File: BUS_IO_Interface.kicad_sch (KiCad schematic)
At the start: 21 parts, among them U12 MAX31331TETB+, U13 AS1016204-0108X0PWAY, U14 TCAN1044ADDFRQ1, Y3 32.768kHz

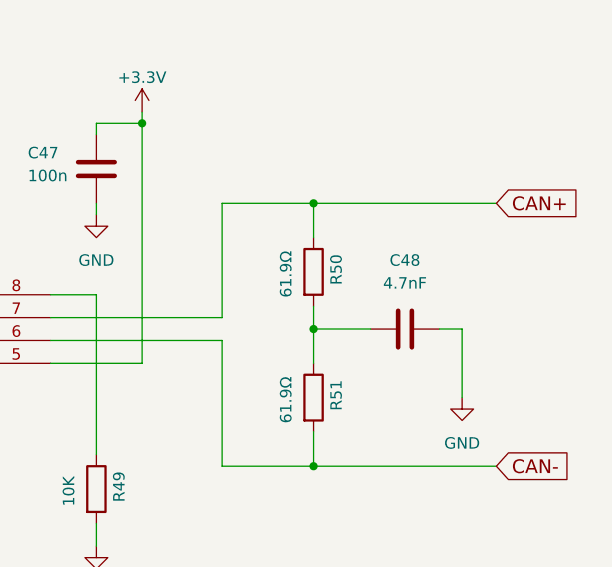
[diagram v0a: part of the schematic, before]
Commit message: Fix values of a lot of parts
Make them standard, 4.1p instead of 4p1, etc.

Add a tag to a couple of ICs that didn't have a pin 1 indicator on the
board.

Signed-off-by: Corey Minyard <corey@minyard.net>
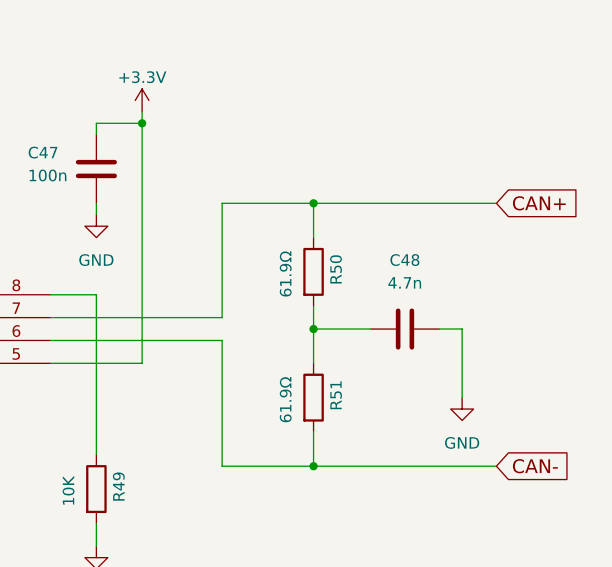
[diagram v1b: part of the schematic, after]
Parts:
- C48: value 4.7nF -> 4.7n
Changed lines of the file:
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@@
 			)
 		)
-		(property "Value" "4.7nF"
+		(property "Value" "4.7n"
 			(at 358.14 91.44 90)
 			(effects

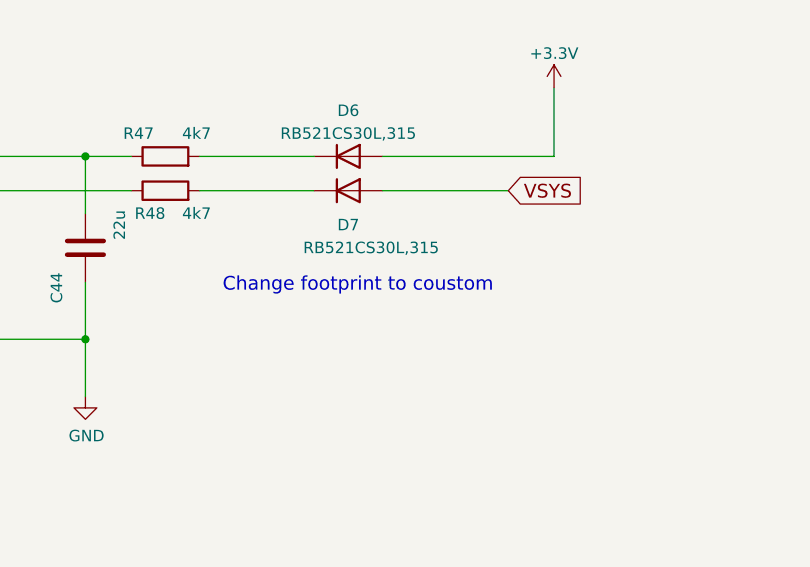
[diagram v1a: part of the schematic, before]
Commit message: Add some notes, fix the diode footprints on the RTC
Signed-off-by: Corey Minyard <corey@minyard.net>
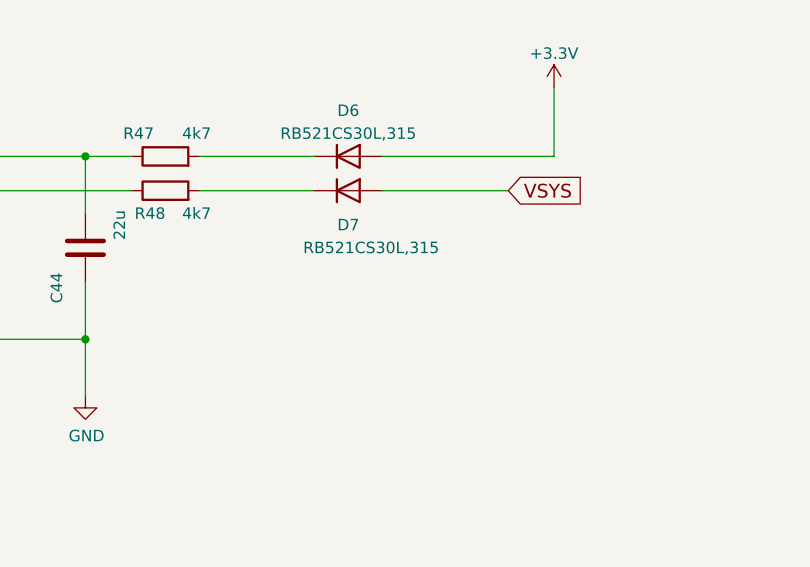
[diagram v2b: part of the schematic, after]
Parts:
- D6, D7: footprint Diode_SMD:D_0603_1608Metric -> Diode_SMD:D_SOD-882
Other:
- note removed: "Change footprint to coustom"
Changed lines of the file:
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@@
 		)
 	)
-	(text "Change footprint to coustom"
-		(exclude_from_sim no)
-		(at 186.69 161.29 0)
-		(effects
-			(font
-				(size 1.524 1.524)
-			)
-			(justify left bottom)
-		)
-	)
 	(text "Real Time Clock"
 		(exclude_from_sim no)
@@
 			)
 		)
-		(property "Footprint" "Diode_SMD:D_0603_1608Metric"
+		(property "Footprint" "Diode_SMD:D_SOD-882"
 			(at 200.66 150.495 0)
 			(effects
@@
 			)
 		)
-		(property "Footprint" "Diode_SMD:D_0603_1608Metric"
+		(property "Footprint" "Diode_SMD:D_SOD-882"
 			(at 200.66 154.305 0)
 			(effects

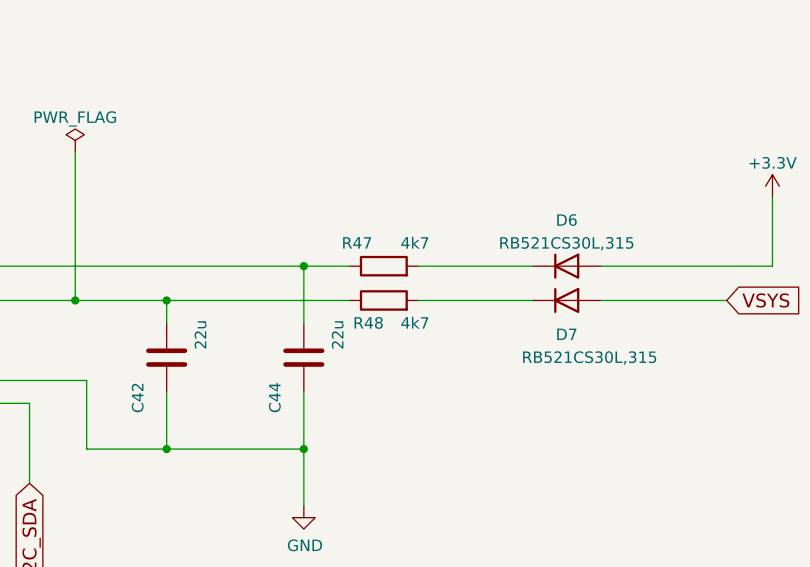
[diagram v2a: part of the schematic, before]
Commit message: Update ferrite beads with actual values
Signed-off-by: Corey Minyard <corey@minyard.net>
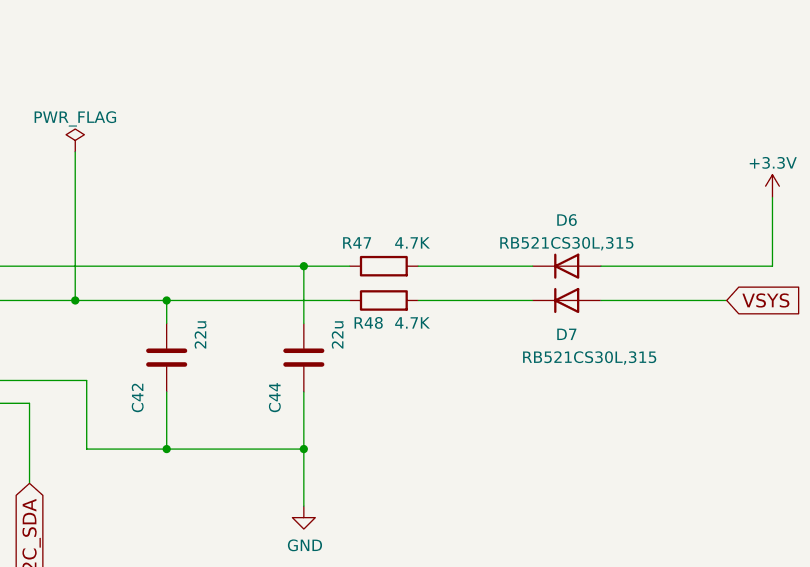
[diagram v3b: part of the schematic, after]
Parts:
- R47, R48: value 4k7 -> 4.7K
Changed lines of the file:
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@@
 			)
 		)
-		(property "Value" "4k7"
+		(property "Value" "4.7K"
 			(at 185.42 143.51 90)
 			(effects
@@
 			)
 		)
-		(property "Value" "4k7"
+		(property "Value" "4.7K"
 			(at 185.42 152.4 90)
 			(effects

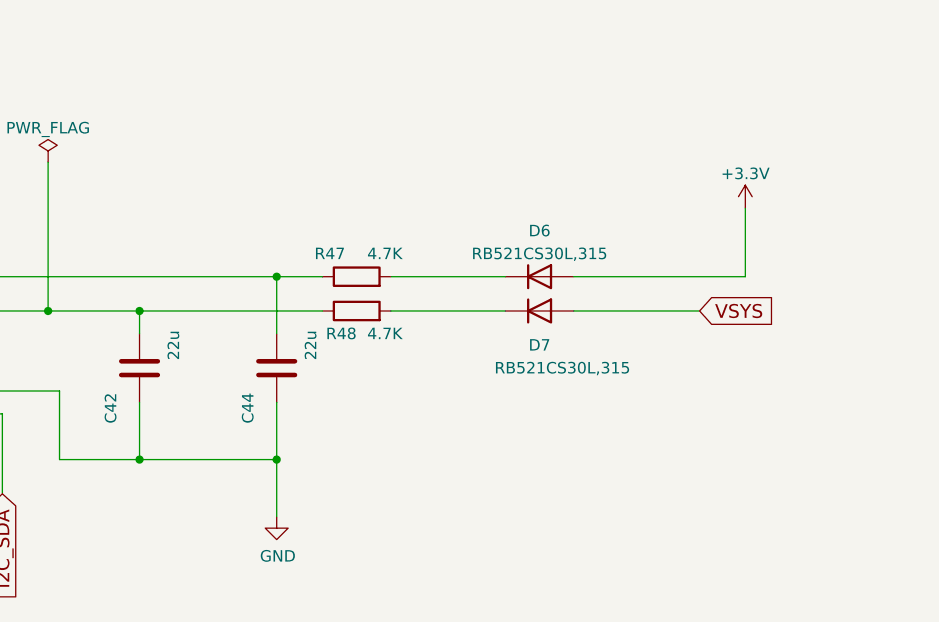
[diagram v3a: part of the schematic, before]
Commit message: Move the RTC and rework it a bit
Signed-off-by: Corey Minyard <corey@minyard.net>
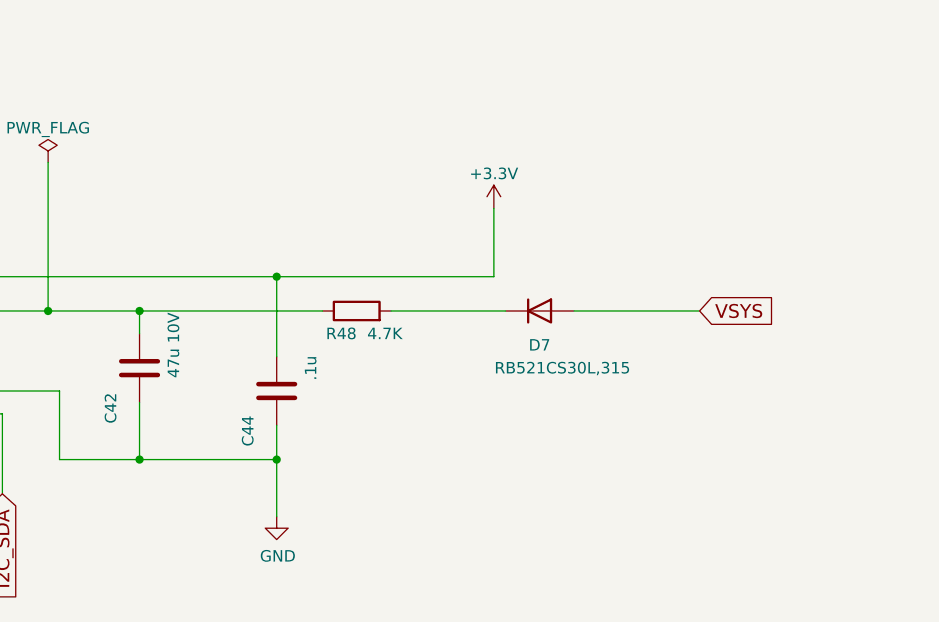
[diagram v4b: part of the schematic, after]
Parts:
- removed D6: RB521CS30L,315, Diode_SMD:D_SOD-882, symbol Diode:1N914
- removed R47: 4.7K, Resistor_SMD:R_0603_1608Metric_Pad0.98x0.95mm_HandSolder, symbol Device:R
- C42: value 22u -> 47u 10V; footprint Capacitor_SMD:C_0603_1608Metric_Pad1.08x0.95mm_HandSolder -> Capacitor_SMD:C_0805_2012Metric_Pad1.18x1.45mm_HandSolder
- C44: value 22u -> .1u
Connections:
- net +3.3V: now also C44.1, U12.10 (VCC)
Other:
- moved on the sheet: C44
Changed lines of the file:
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@@
-	(wire
-		(pts
-			(xy 184.15 146.05) (xy 196.85 146.05)
-		)
-		(stroke
-			(width 0)
-			(type default)
-		)
-	)
 	(wire
 		(pts
@@
 	(wire
 		(pts
-			(xy 171.45 146.05) (xy 176.53 146.05)
+			(xy 171.45 146.05) (xy 195.58 146.05)
 		)
 		(stroke
@@
 	(wire
 		(pts
-			(xy 171.45 146.05) (xy 171.45 152.4)
+			(xy 171.45 146.05) (xy 171.45 154.94)
 		)
 		(stroke
@@
 	(wire
 		(pts
-			(xy 171.45 166.37) (xy 171.45 160.02)
+			(xy 171.45 166.37) (xy 171.45 162.56)
 		)
 		(stroke
@@
 	(wire
 		(pts
-			(xy 223.52 146.05) (xy 223.52 138.43)
+			(xy 195.58 146.05) (xy 195.58 138.43)
 		)
 		(stroke
@@
 		(pts
 			(xy 92.71 147.32) (xy 92.71 134.62)
-		)
-		(stroke
-			(width 0)
-			(type default)
-		)
-	)
-	(wire
-		(pts
-			(xy 204.47 146.05) (xy 223.52 146.05)
 		)
 		(stroke
@@
 			)
 		)
-		(property "Value" "22u"
+		(property "Value" "47u 10V"
 			(at 160.02 153.67 90)
 			(effects
@@
 			)
 		)
-		(property "Footprint" "Capacitor_SMD:C_0603_1608Metric_Pad1.08x0.95mm_HandSolder"
+		(property "Footprint" "Capacitor_SMD:C_0805_2012Metric_Pad1.18x1.45mm_HandSolder"
 			(at 157.1752 160.02 0)
 			(effects
@@
 	)
 	(symbol
-		(lib_id "Device:R")
-		(at 180.34 146.05 90)
-		(unit 1)
-		(exclude_from_sim no)
-		(in_bom yes)
-		(on_board yes)
-		(dnp no)
-		(property "Reference" "R47"
-			(at 179.07 143.51 90)
-			(effects
-				(font
-					(size 1.27 1.27)
-				)
-				(justify left)
-			)
-		)
-		(property "Value" "4.7K"
-			(at 185.42 143.51 90)
-			(effects
-				(font
-					(size 1.27 1.27)
-				)
-				(justify left)
-			)
-		)
-		(property "Footprint" "Resistor_SMD:R_0603_1608Metric_Pad0.98x0.95mm_HandSolder"
-			(at 180.34 147.828 90)
-			(effects
-				(font
-					(size 1.27 1.27)
-				)
-				(hide yes)
-			)
-		)
-		(property "Datasheet" "~"
-			(at 180.34 146.05 0)
-			(effects
-				(font
-					(size 1.27 1.27)
-				)
-			)
-		)
-		(property "Description" ""
-			(at 180.34 146.05 0)
-			(effects
-				(font
-					(size 1.27 1.27)
-				)
-			)
-		)
-		(pin "1"
-		)
-		(pin "2"
-		)
-		(instances
-			(project "PacSat_Dev_RevD_240614"
-				(path "/cc9f42d2-6985-41ac-acab-5ab7b01c5b38/aff81ec5-748c-4fc9-b1e8-df12a16f6289"
-					(reference "R47")
-					(unit 1)
-				)
-			)
-		)
-	)
-	(symbol
 		(lib_id "PACSAT_ICs:MAX31331")
 		(at 110.49 154.94 0)
@@
 	(symbol
 		(lib_id "Device:C")
-		(at 171.45 156.21 0)
+		(at 171.45 158.75 0)
 		(unit 1)
 		(exclude_from_sim no)
@@
 		(dnp no)
 		(property "Reference" "C44"
-			(at 168.275 160.655 90)
-			(effects
-				(font
-					(size 1.27 1.27)
-				)
-			)
-		)
-		(property "Value" "22u"
-			(at 175.26 153.67 90)
+			(at 168.275 163.195 90)
+			(effects
+				(font
+					(size 1.27 1.27)
+				)
+			)
+		)
+		(property "Value" ".1u"
+			(at 175.26 156.21 90)
 			(effects
 				(font
@@
 		)
 		(property "Footprint" "Capacitor_SMD:C_0603_1608Metric_Pad1.08x0.95mm_HandSolder"
-			(at 172.4152 160.02 0)
+			(at 172.4152 162.56 0)
 			(effects
 				(font
@@
 		)
 		(property "Datasheet" "~"
-			(at 171.45 156.21 0)
+			(at 171.45 158.75 0)
 			(effects
 				(font
@@
 		)
 		(property "Description" ""
-			(at 171.45 156.21 0)
+			(at 171.45 158.75 0)
 			(effects
 				(font
@@
 	)
 	(symbol
-		(lib_id "Diode:1N914")
-		(at 200.66 146.05 0)
-		(unit 1)
-		(exclude_from_sim no)
-		(in_bom yes)
-		(on_board yes)
-		(dnp no)
-		(fields_autoplaced yes)
-		(property "Reference" "D6"
-			(at 200.66 140.97 0)
-			(effects
-				(font
-					(size 1.27 1.27)
-				)
-			)
-		)
-		(property "Value" "RB521CS30L,315"
-			(at 200.66 143.51 0)
-			(effects
-				(font
-					(size 1.27 1.27)
-				)
-			)
-		)
-		(property "Footprint" "Diode_SMD:D_SOD-882"
-			(at 200.66 150.495 0)
-			(effects
-				(font
-					(size 1.27 1.27)
-				)
-				(hide yes)
-			)
-		)
-		(property "Datasheet" "http://www.vishay.com/docs/85622/1n914.pdf"
-			(at 200.66 146.05 0)
-			(effects
-				(font
-					(size 1.27 1.27)
-				)
-				(hide yes)
-			)
-		)
-		(property "Description" ""
-			(at 200.66 146.05 0)
-			(effects
-				(font
-					(size 1.27 1.27)
-				)
-			)
-		)
-		(property "Sim.Device" "D"
-			(at 200.66 146.05 0)
-			(effects
-				(font
-					(size 1.27 1.27)
-				)
-				(hide yes)
-			)
-		)
-		(property "Sim.Pins" "1=K 2=A"
-			(at 200.66 146.05 0)
-			(effects
-				(font
-					(size 1.27 1.27)
-				)
-				(hide yes)
-			)
-		)
-		(pin "1"
-		)
-		(pin "2"
-		)
-		(instances
-			(project "PacSat_Dev_RevD_240614"
-				(path "/cc9f42d2-6985-41ac-acab-5ab7b01c5b38/aff81ec5-748c-4fc9-b1e8-df12a16f6289"
-					(reference "D6")
-					(unit 1)
-				)
-			)
-		)
-	)
-	(symbol
 		(lib_id "PACSAT_ICs:QSPI_FLASH_WSON_8-pin")
 		(at 133.35 64.77 0)
@@
 	(symbol
 		(lib_id "power:+3.3V")
-		(at 223.52 138.43 0)
+		(at 195.58 138.43 0)
 		(unit 1)
 		(exclude_from_sim no)
@@
 		(fields_autoplaced yes)
 		(property "Reference" "#PWR0113"
-			(at 223.52 142.24 0)
+			(at 195.58 142.24 0)
 			(effects
 				(font
@@
 		)
 		(property "Value" "+3.3V"
-			(at 223.52 134.62 0)
+			(at 195.58 134.62 0)
 			(effects
 				(font
@@
 		)
 		(property "Footprint" ""
-			(at 223.52 138.43 0)
+			(at 195.58 138.43 0)
 			(effects
 				(font
@@
 		)
 		(property "Datasheet" ""
-			(at 223.52 138.43 0)
+			(at 195.58 138.43 0)
 			(effects
 				(font
@@
 		)
 		(property "Description" ""
-			(at 223.52 138.43 0)
-			(effects
-				(font
+			(at 195.58 138.43 0)
+			(effects
+				(font

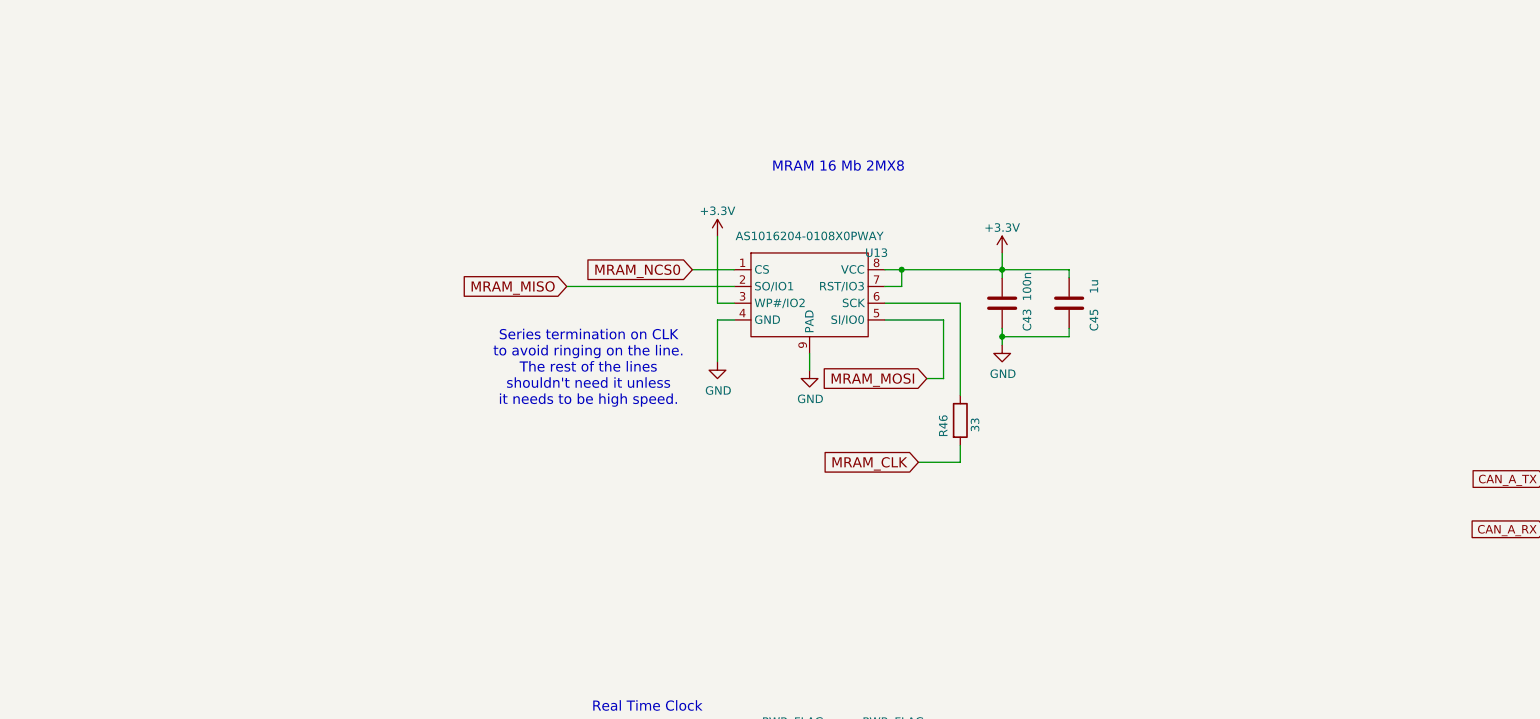
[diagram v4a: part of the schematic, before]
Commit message: Add 4 more MRAM parts
Signed-off-by: Corey Minyard <corey@minyard.net>
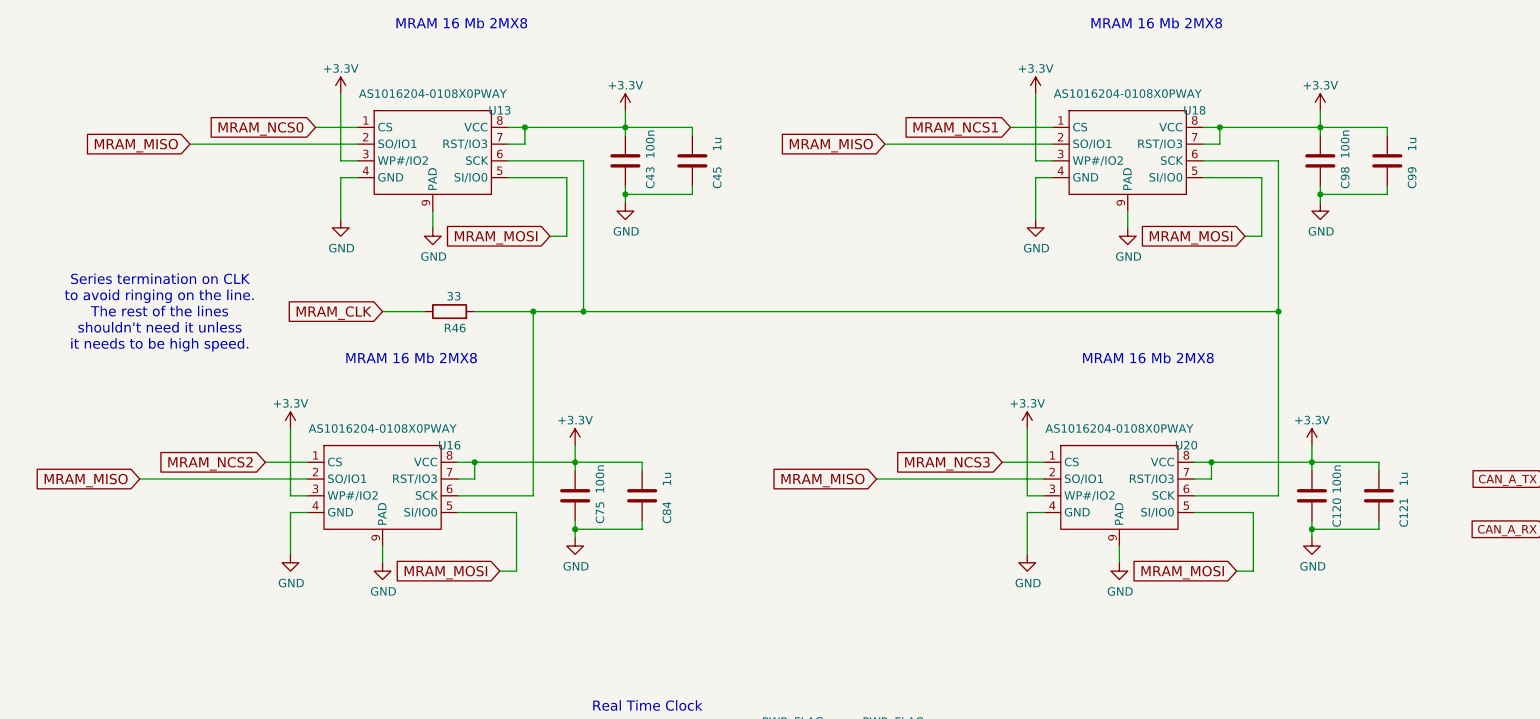
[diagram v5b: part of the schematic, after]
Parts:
- added C120, C75, C98: 100n, Capacitor_SMD:C_0603_1608Metric_Pad1.08x0.95mm_HandSolder, symbol Device:C
- added C121, C84, C99: 1u, Capacitor_SMD:C_0603_1608Metric_Pad1.08x0.95mm_HandSolder, symbol Device:C
- added U16, U18, U20: AS1016204-0108X0PWAY, Package_SON:WSON-8-1EP_8x6mm_P1.27mm_EP3.4x4.3mm, symbol PACSAT_ICs:QSPI_FLASH_WSON_8-pin
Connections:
- net +3.3V: now also C120.1, C121.1, C75.1, C84.1, C98.1, C99.1, U16.3 (WP#/IO2), U16.7 (RST/IO3), U16.8 (VCC), U18.3 (WP#/IO2), U18.7 (RST/IO3), U18.8 (VCC), U20.3 (WP#/IO2), U20.7 (RST/IO3), U20.8 (VCC)
- net GND: now also C120.2, C121.2, C75.2, C84.2, C98.2, C99.2, U16.4 (GND), U16.9 (PAD), U18.4 (GND), U18.9 (PAD), U20.4 (GND), U20.9 (PAD)
- net MRAM_CLK: now also R46.1; no longer R46.2
- net MRAM_MISO: now also U16.2 (SO/IO1), U18.2 (SO/IO1), U20.2 (SO/IO1)
- net MRAM_MOSI: now also U16.5 (SI/IO0), U18.5 (SI/IO0), U20.5 (SI/IO0)
- net at U13.6 (SCK): now also R46.2, U16.6 (SCK), U18.6 (SCK), U20.6 (SCK); no longer R46.1
- new net MRAM_NCS1: U18.1 (CS)
- new net MRAM_NCS2: U16.1 (CS)
- new net MRAM_NCS3: U20.1 (CS)
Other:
- moved on the sheet: C43, C45, R46, U13
